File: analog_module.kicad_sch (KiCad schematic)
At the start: 9 parts

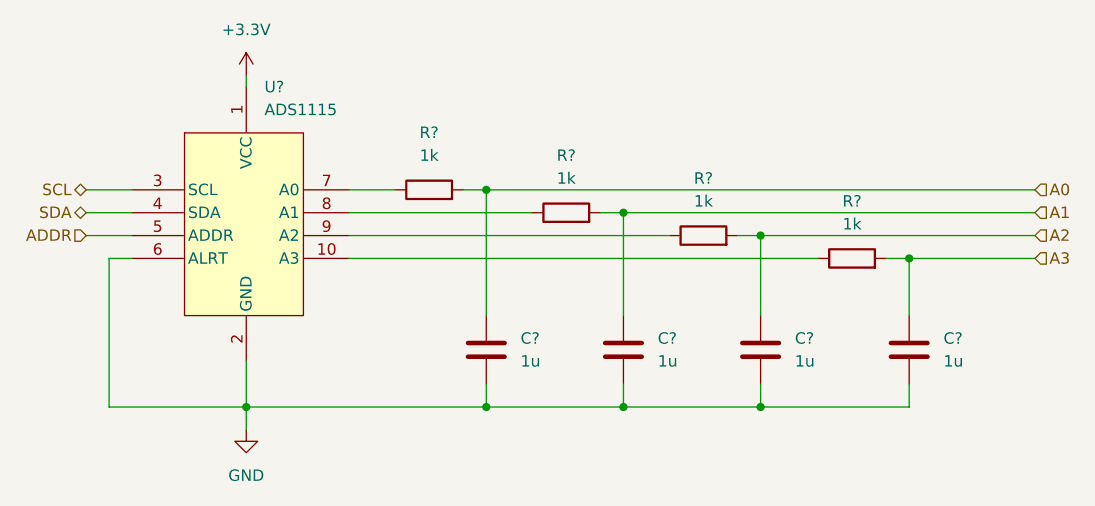
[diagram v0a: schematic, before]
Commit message: added power loss detection, preparing for new pcb layout
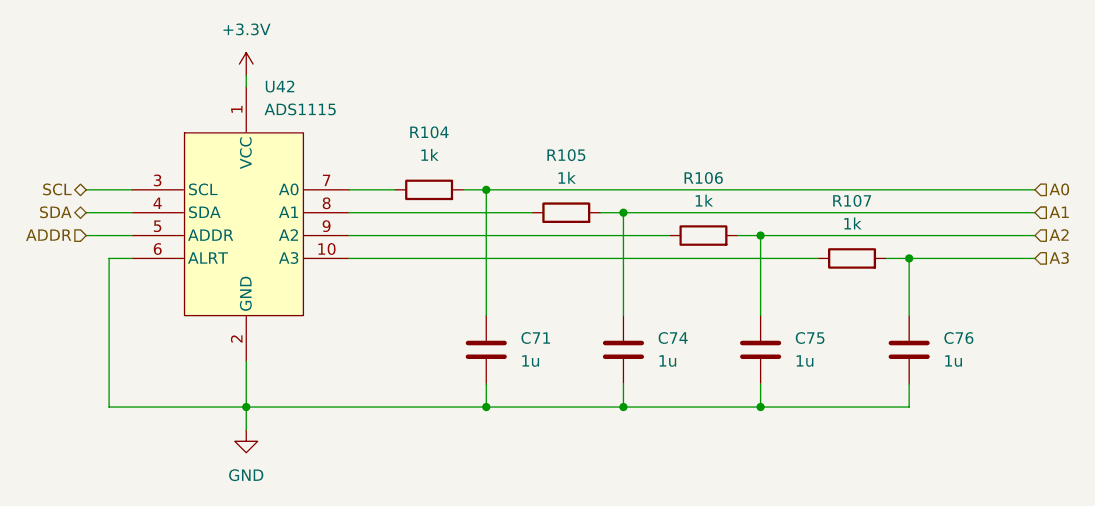
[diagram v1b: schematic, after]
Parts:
- gave numbers to parts that had none: 9
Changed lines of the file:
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@@
   (symbol (lib_id "power:+3.3V") (at 111.76 76.2 0) (unit 1)
     (in_bom yes) (on_board yes) (fields_autoplaced)
-    (property "Reference" "#PWR?" (id 0) (at 111.76 80.01 0)
+    (property "Reference" "#PWR0175" (id 0) (at 111.76 80.01 0)
       (effects (font (size 1.27 1.27)) hide)
     )
@@
   (symbol (lib_id "Device:R") (at 162.56 93.98 90) (unit 1)
     (in_bom yes) (on_board yes) (fields_autoplaced)
-    (property "Reference" "R?" (id 0) (at 162.56 87.63 90))
+    (property "Reference" "R106" (id 0) (at 162.56 87.63 90))
     (property "Value" "1k" (id 1) (at 162.56 90.17 90))
     (property "Footprint" "Resistor_SMD:R_0603_1608Metric_Pad0.98x0.95mm_HandSolder" (id 2) (at 162.56 95.758 90)
@@
   (symbol (lib_id "power:GND") (at 111.76 115.57 0) (unit 1)
     (in_bom yes) (on_board yes) (fields_autoplaced)
-    (property "Reference" "#PWR?" (id 0) (at 111.76 121.92 0)
+    (property "Reference" "#PWR0168" (id 0) (at 111.76 121.92 0)
       (effects (font (size 1.27 1.27)) hide)
     )
@@
   (symbol (lib_id "Device:R") (at 147.32 91.44 90) (unit 1)
     (in_bom yes) (on_board yes) (fields_autoplaced)
-    (property "Reference" "R?" (id 0) (at 147.32 85.09 90))
+    (property "Reference" "R105" (id 0) (at 147.32 85.09 90))
     (property "Value" "1k" (id 1) (at 147.32 87.63 90))
     (property "Footprint" "Resistor_SMD:R_0603_1608Metric_Pad0.98x0.95mm_HandSolder" (id 2) (at 147.32 93.218 90)
@@
   (symbol (lib_id "Device:R") (at 132.08 88.9 90) (unit 1)
     (in_bom yes) (on_board yes) (fields_autoplaced)
-    (property "Reference" "R?" (id 0) (at 132.08 82.55 90))
+    (property "Reference" "R104" (id 0) (at 132.08 82.55 90))
     (property "Value" "1k" (id 1) (at 132.08 85.09 90))
     (property "Footprint" "Resistor_SMD:R_0603_1608Metric_Pad0.98x0.95mm_HandSolder" (id 2) (at 132.08 90.678 90)
@@
   (symbol (lib_id "_Modules:ADS1115") (at 111.76 92.71 0) (unit 1)
     (in_bom yes) (on_board yes) (fields_autoplaced)
-    (property "Reference" "U?" (id 0) (at 113.7794 77.47 0)
+    (property "Reference" "U42" (id 0) (at 113.7794 77.47 0)
       (effects (font (size 1.27 1.27)) (justify left))
     )
@@
   (symbol (lib_id "Device:C") (at 168.91 106.68 0) (unit 1)
     (in_bom yes) (on_board yes) (fields_autoplaced)
-    (property "Reference" "C?" (id 0) (at 172.72 105.4099 0)
+    (property "Reference" "C75" (id 0) (at 172.72 105.4099 0)
       (effects (font (size 1.27 1.27)) (justify left))
     )
@@
   (symbol (lib_id "Device:C") (at 153.67 106.68 0) (unit 1)
     (in_bom yes) (on_board yes) (fields_autoplaced)
-    (property "Reference" "C?" (id 0) (at 157.48 105.4099 0)
+    (property "Reference" "C74" (id 0) (at 157.48 105.4099 0)
       (effects (font (size 1.27 1.27)) (justify left))
     )
@@
   (symbol (lib_id "Device:C") (at 138.43 106.68 0) (unit 1)
     (in_bom yes) (on_board yes) (fields_autoplaced)
-    (property "Reference" "C?" (id 0) (at 142.24 105.4099 0)
+    (property "Reference" "C71" (id 0) (at 142.24 105.4099 0)
       (effects (font (size 1.27 1.27)) (justify left))
     )
@@
   (symbol (lib_id "Device:R") (at 179.07 96.52 90) (unit 1)
     (in_bom yes) (on_board yes) (fields_autoplaced)
-    (property "Reference" "R?" (id 0) (at 179.07 90.17 90))
+    (property "Reference" "R107" (id 0) (at 179.07 90.17 90))
     (property "Value" "1k" (id 1) (at 179.07 92.71 90))
     (property "Footprint" "Resistor_SMD:R_0603_1608Metric_Pad0.98x0.95mm_HandSolder" (id 2) (at 179.07 98.298 90)
@@
   (symbol (lib_id "Device:C") (at 185.42 106.68 0) (unit 1)
     (in_bom yes) (on_board yes) (fields_autoplaced)
-    (property "Reference" "C?" (id 0) (at 189.23 105.4099 0)
+    (property "Reference" "C76" (id 0) (at 189.23 105.4099 0)
       (effects (font (size 1.27 1.27)) (justify left))
     )
